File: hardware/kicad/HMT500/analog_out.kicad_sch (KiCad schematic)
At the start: 20 parts, among them U10 TPS26611, U7 DAC8760IPWP, U8 DAC8760IPWP, U9 TPS26611

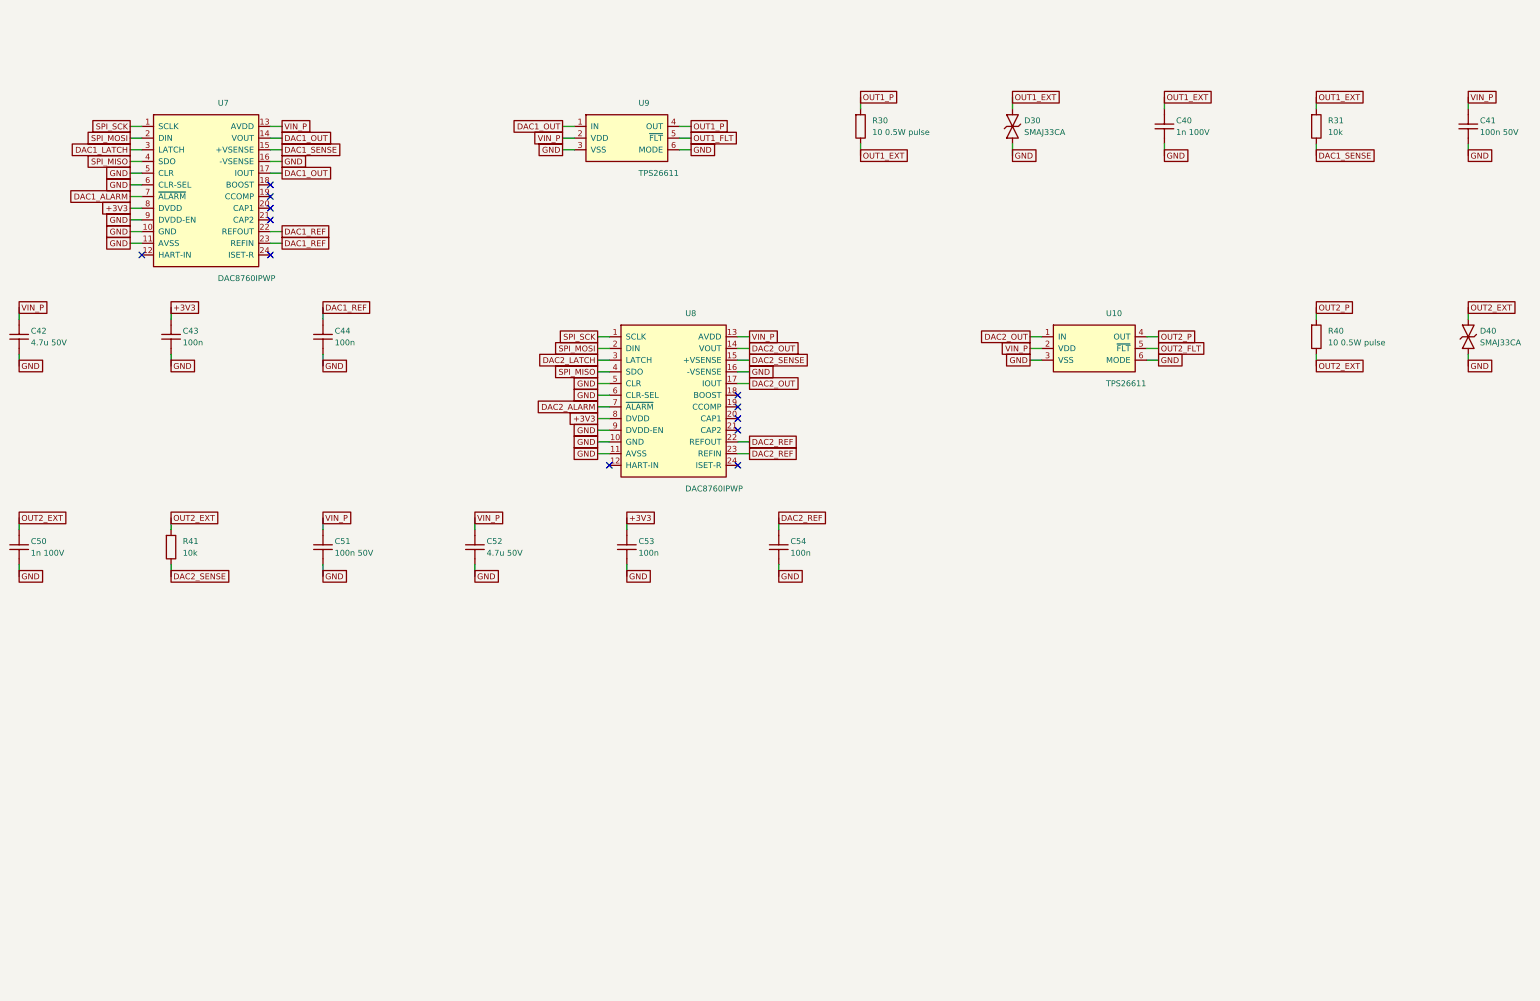
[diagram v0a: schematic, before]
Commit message: KiCad schematic v0.2: hand-laid-out, wired, readable sheets with power symbols and functional blocks
Replaces the label-only v0.1. Drawing rules are validated at generation and
the drawn netlist is checked against design intent (71 nets, 0 errors).

Co-Authored-By: Claude Opus 5.5 <noreply@anthropic.com>
Claude-Session: https://claude.ai/code/session_01JA2o8uJsqp9Vzsg4b665ev
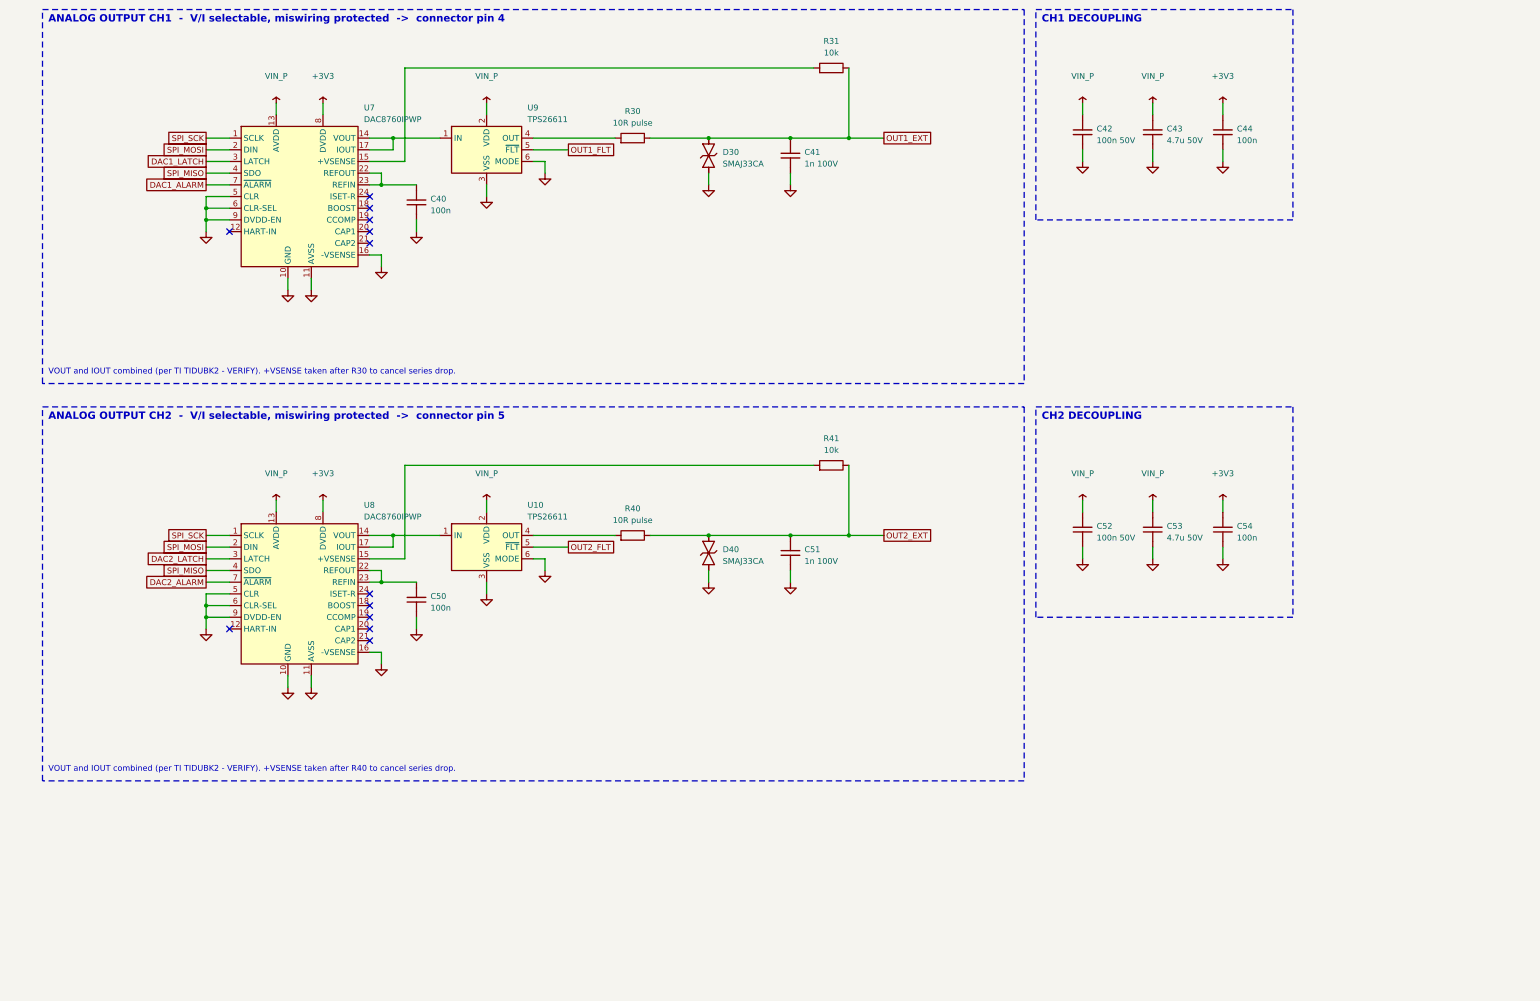
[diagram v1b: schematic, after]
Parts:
- C40, C50: value 1n 100V -> 100n
- C41, C51: value 100n 50V -> 1n 100V; footprint Capacitor_SMD:C_0805_2012Metric -> Capacitor_SMD:C_0603_1608Metric
- C42, C52: value 4.7u 50V -> 100n 50V; footprint Capacitor_SMD:C_1206_3216Metric -> Capacitor_SMD:C_0805_2012Metric
- C43, C53: value 100n -> 4.7u 50V; footprint Capacitor_SMD:C_0603_1608Metric -> Capacitor_SMD:C_1210_3225Metric
- R30, R40: value 10 0.5W pulse -> 10R pulse
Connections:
- net +3V3: now also C44.1, C54.1; no longer C43.1, C53.1
- net OUT1_EXT: now also C41.1, R31.2; no longer C40.1, R31.1
- net OUT2_EXT: now also C51.1, R41.2; no longer C50.1, R41.1
- net VIN_P: now also C43.1, C53.1; no longer C41.1, C51.1
- net DAC1_OUT: no longer names the net of U7.14 (VOUT), U7.17 (IOUT), U9.1 (IN)
- net DAC1_REF: no longer names the net of U7.22 (REFOUT), U7.23 (REFIN)
- net DAC1_REF: now also C40.1; no longer C44.1
- net DAC1_SENSE: no longer names the net of U7.15 (+VSENSE)
- net DAC1_SENSE: now also R31.1; no longer R31.2
- net DAC2_OUT: no longer names the net of U10.1 (IN), U8.14 (VOUT), U8.17 (IOUT)
- net DAC2_REF: no longer names the net of U8.22 (REFOUT), U8.23 (REFIN)
- net DAC2_REF: now also C50.1; no longer C54.1
- net DAC2_SENSE: no longer names the net of U8.15 (+VSENSE)
- net DAC2_SENSE: now also R41.1; no longer R41.2
- net OUT1_P: no longer names the net of R30.1, U9.4 (OUT)
- net OUT2_P: no longer names the net of R40.1, U10.4 (OUT)
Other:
- note added: "ANALOG OUTPUT CH1 - V/I selectable, miswiring protected -> connector pin 4"
- note added: "ANALOG OUTPUT CH2 - V/I selectable, miswiring protected -> connector pin 5"
- note added: "CH1 DECOUPLING"
- note added: "CH2 DECOUPLING"
- note added: "VOUT and IOUT combined (per TI TIDUBK2 - VERIFY). +VSENSE taken after R30 to cancel series drop."
- note added: "VOUT and IOUT combined (per TI TIDUBK2 - VERIFY). +VSENSE taken after R40 to cancel series drop."
- title: HMT500 - Analog outputs x2 (V/I selectable) with miswiring protection -> HMT500  Analog outputs
- moved on the sheet: C40, C41, C42, C43, C44, C50, C51, C52, C53, C54, R30, R31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

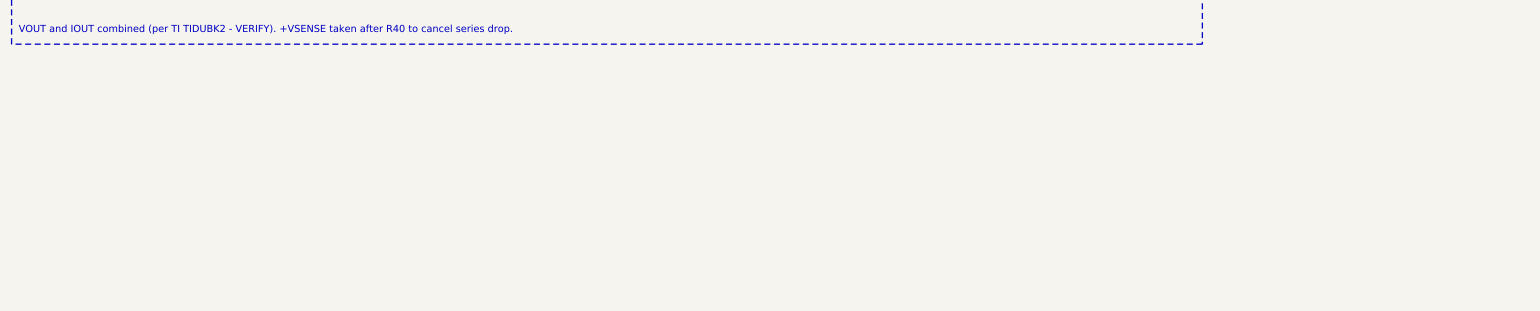
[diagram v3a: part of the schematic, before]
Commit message: Record DAC decision: keep DAC8760, list drop-in alternates
Keep DAC8760 fitted on U7/U8 for now. Once the output spec is fixed,
fit a pin-compatible alternate from the same family: DAC7760 (12-bit
V/I), DAC8750 (16-bit current only) or DAC7750 (12-bit current only).
A "DAC SELECTION" note on the analog output sheet records this, and
the parts list U7/U8 description mentions the alternates. The title
block verify note is shortened.

Add docs/decision-log.md, a dated log of decisions made so far (comms,
connector, pinout, protection, mech Rev B/C, in-house parts policy,
MCU, DAC) and open items.

Co-Authored-By: Claude Opus 5.5 <noreply@anthropic.com>
Claude-Session: https://claude.ai/code/session_01JA2o8uJsqp9Vzsg4b665ev
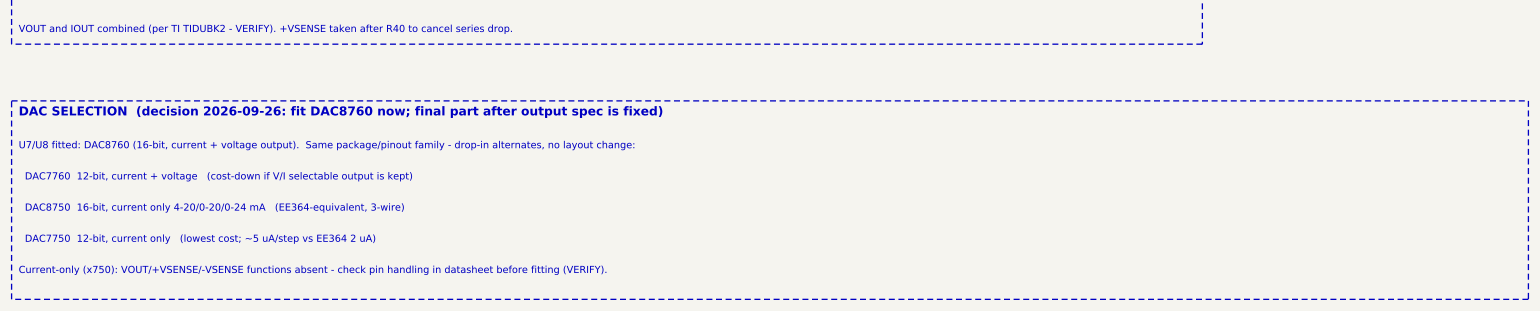
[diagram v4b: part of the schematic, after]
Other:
- note added: "Current-only (x750): VOUT/+VSENSE/-VSENSE functions absent - check pin handling in datasheet before fitting (VERIFY)."
- note added: "DAC SELECTION (decision 2026-09-26: fit DAC8760 now; final part after output spec is fixed)"
- note added: "DAC7750 12-bit, current only (lowest cost; ~5 uA/step vs EE364 2 uA)"
- note added: "DAC7760 12-bit, current + voltage (cost-down if V/I selectable output is kept)"
- note added: "DAC8750 16-bit, current only 4-20/0-20/0-24 mA (EE364-equivalent, 3-wire)"
- note added: "U7/U8 fitted: DAC8760 (16-bit, current + voltage output). Same package/pinout family - drop-in alternates, no layout change:"
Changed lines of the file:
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@@
 (kicad_sch (version 20230121) (generator eeschema) (paper "A3")
-(title_block (title "HMT500  Analog outputs") (date "2026-09-26") (rev "0.3") (company "DOTECH Co., Ltd.") (comment 1 "Oil moisture transmitter HMT500 - RS-485 + 2x V/I analog output") (comment 2 "Design notes: docs/hw/circuit-design.md") (comment 3 "VERIFY=YES parts: placeholder pin numbers (LMR36006, PCAP04, DAC8760, TPS26611); TPS2660 RTN wiring"))
+(title_block (title "HMT500  Analog outputs") (date "2026-09-26") (rev "0.3") (company "DOTECH Co., Ltd.") (comment 1 "Oil moisture transmitter HMT500 - RS-485 + 2x V/I analog output") (comment 2 "Design notes: docs/hw/circuit-design.md") (comment 3 "VERIFY=YES parts: pin numbers LMR36006/PCAP04/DAC8760/TPS26611; TPS2660 R22"))
 (symbol (lib_id "HMT500:DAC8760") (at 86.36 55.88 0) (unit 1) (in_bom yes) (on_board yes) (dnp no) (property "Reference" "U7" (at 100.33 36.576 0) (effects (font (size 1.27 1.27)) (justify left))) (property "Value" "DAC8760IPWP" (at 100.33 39.116 0) (effects (font (size 1.27 1.27)) (justify left))) (property "Footprint" "TBD:HTSSOP-24_DAC8760" (at 86.36 55.88 0) (effects (font (size 1.27 1.27)) hide)) (property "Datasheet" "~" (at 86.36 55.88 0) (effects (font (size 1.27 1.27)) hide)) (property "VERIFY" "YES - pin numbers are placeholders" (at 86.36 55.88 0) (effects (font (size 1.27 1.27)) hide)) (pin "1") (pin "2") (pin "3") (pin "4") (pin "7") (pin "5") (pin "6") (pin "9") (pin "12") (pin "14") (pin "17") (pin "15") (pin "22") (pin "23") (pin "24") (pin "18") (pin "19") (pin "20") (pin "21") (pin "16") (pin "13") (pin "8") (pin "10") (pin "11") (instances (project "HMT500" (path "/1ebb025b-11bd-5f7c-aaab-41e2a750e8b3/41cd7a48-3e3d-5ed7-a9e3-c51ab363ff56" (reference "U7") (unit 1)))))
 (symbol (lib_id "HMT500:GND") (at 66.04 63.5 0) (unit 1) (in_bom no) (on_board no) (dnp no) (property "Reference" "#PWR080" (at 66.04 69.85 0) (effects (font (size 1.27 1.27)) hide)) (property "Value" "GND" (at 66.04 71.12 0) (effects (font (size 1.27 1.27)) hide)) (property "Footprint" "" (at 66.04 63.5 0) (effects (font (size 1.27 1.27)) hide)) (property "Datasheet" "~" (at 66.04 63.5 0) (effects (font (size 1.27 1.27)) hide)) (pin "1") (instances (project "HMT500" (path "/1ebb025b-11bd-5f7c-aaab-41e2a750e8b3/41cd7a48-3e3d-5ed7-a9e3-c51ab363ff56" (reference "#PWR080") (unit 1)))))
@@
 (rectangle (start 30.48 101.6) (end 243.84 182.88) (stroke (width 0.1524) (type dash) (color 72 72 160 1)) (fill (type none)))
 (rectangle (start 246.38 101.6) (end 302.26 147.32) (stroke (width 0.1524) (type dash) (color 72 72 160 1)) (fill (type none)))
+(rectangle (start 30.48 193.04) (end 302.26 228.6) (stroke (width 0.1524) (type dash) (color 72 72 160 1)) (fill (type none)))
 (text "ANALOG OUTPUT CH1  -  V/I selectable, miswiring protected  ->  connector pin 4" (at 31.75 18.288 0) (effects (font (size 1.6 1.6) bold) (justify left bottom)))
 (text "VOUT and IOUT combined (per TI TIDUBK2 - VERIFY). +VSENSE taken after R30 to cancel series drop." (at 31.75 94.742 0) (effects (font (size 1.27 1.27)) (justify left bottom)))
@@
 (text "VOUT and IOUT combined (per TI TIDUBK2 - VERIFY). +VSENSE taken after R40 to cancel series drop." (at 31.75 181.102 0) (effects (font (size 1.27 1.27)) (justify left bottom)))
 (text "CH2 DECOUPLING" (at 247.65 104.648 0) (effects (font (size 1.6 1.6) bold) (justify left bottom)))
+(text "DAC SELECTION  (decision 2026-09-26: fit DAC8760 now; final part after output spec is fixed)" (at 31.75 196.088 0) (effects (font (size 1.6 1.6) bold) (justify left bottom)))
+(text "U7/U8 fitted: DAC8760 (16-bit, current + voltage output).  Same package/pinout family - drop-in alternates, no layout change:" (at 31.75 201.93 0) (effects (font (size 1.27 1.27)) (justify left bottom)))
+(text "  DAC7760  12-bit, current + voltage   (cost-down if V/I selectable output is kept)" (at 31.75 207.518 0) (effects (font (size 1.27 1.27)) (justify left bottom)))
+(text "  DAC8750  16-bit, current only 4-20/0-20/0-24 mA   (EE364-equivalent, 3-wire)" (at 31.75 213.106 0) (effects (font (size 1.27 1.27)) (justify left bottom)))
+(text "  DAC7750  12-bit, current only   (lowest cost; ~5 uA/step vs EE364 2 uA)" (at 31.75 218.694 0) (effects (font (size 1.27 1.27)) (justify left bottom)))
+(text "Current-only (x750): VOUT/+VSENSE/-VSENSE functions absent - check pin handling in datasheet before fitting (VERIFY)." (at 31.75 224.282 0) (effects (font (size 1.27 1.27)) (justify left bottom)))
 )
